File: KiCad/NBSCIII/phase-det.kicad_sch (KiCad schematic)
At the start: 34 parts, among them Q1100 BC337-25, U1 LM324N

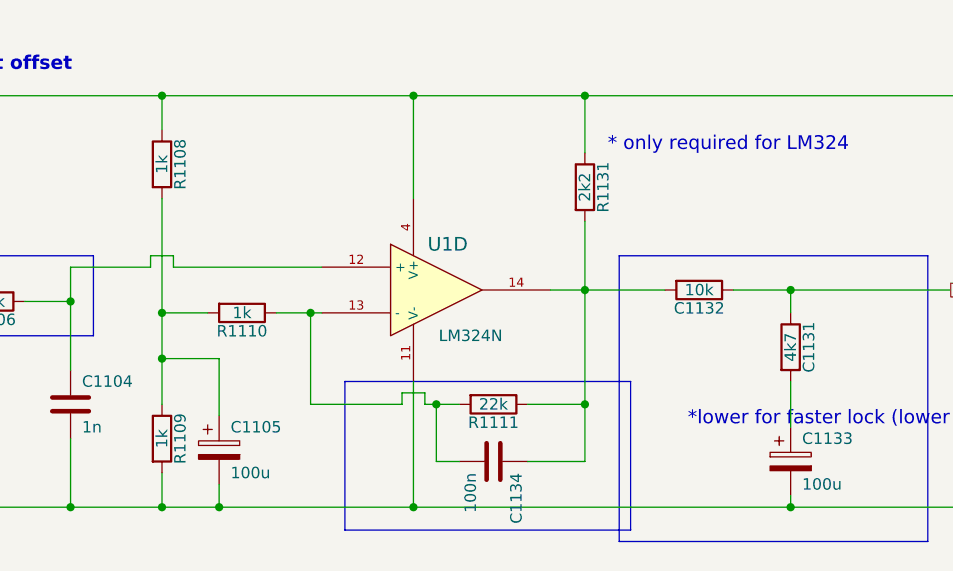
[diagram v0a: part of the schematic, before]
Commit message: derescue lm324
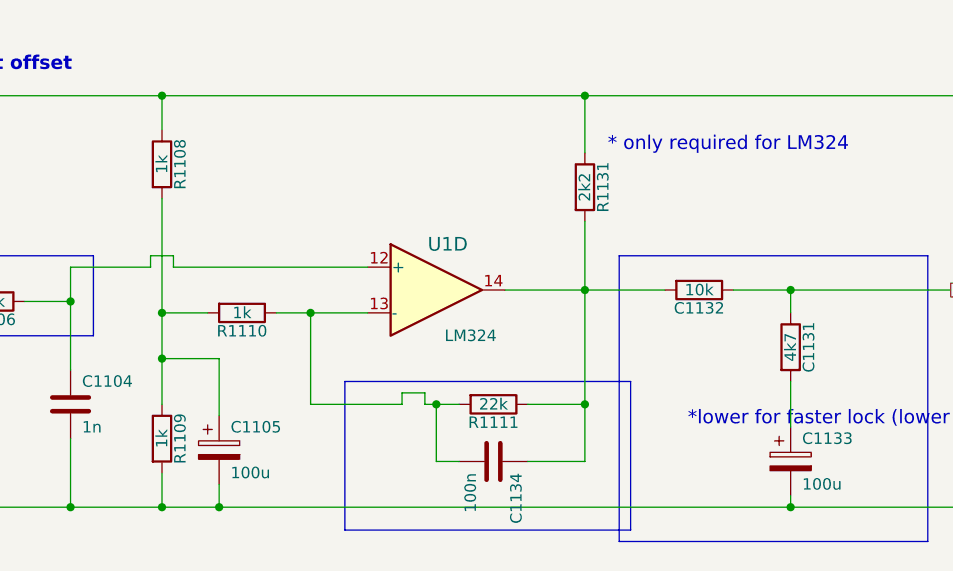
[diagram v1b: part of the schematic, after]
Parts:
- U1: value LM324N -> LM324; symbol NBSCIII-rescue:LM324N -> Amplifier_Operational:LM324
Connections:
- net +12V: no longer U1.4 (V+)
- net GND: no longer U1.11 (V-)
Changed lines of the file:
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@@
   (junction (at 50.8 69.85) (diameter 0) (color 0 0 0 0)
   )
-  (junction (at 179.07 24.13) (diameter 0) (color 0 0 0 0)
-  )
   (junction (at 106.68 46.99) (diameter 0) (color 0 0 0 0)
   )
@@
   (junction (at 220.98 69.85) (diameter 0) (color 0 0 0 0)
   )
-  (junction (at 179.07 69.85) (diameter 0) (color 0 0 0 0)
-  )
   (wire (pts (xy 220.98 69.85) (xy 256.54 69.85))
     (stroke (width 0) (type default) (color 0 0 0 0))
@@
     (stroke (width 0) (type default) (color 0 0 0 0))
   )
+  (wire (pts (xy 152.4 43.18) (xy 173.99 43.18))
+    (stroke (width 0) (type default) (color 0 0 0 0))
+  )
   (wire (pts (xy 151.13 48.26) (xy 156.21 48.26))
     (stroke (width 0) (type default) (color 0 0 0 0))
@@
     (stroke (width 0) (type default) (color 0 0 0 0))
   )
-  (wire (pts (xy 167.64 48.26) (xy 168.91 48.26))
-    (stroke (width 0) (type default) (color 0 0 0 0))
-  )
   (wire (pts (xy 124.46 25.4) (xy 125.73 25.4))
     (stroke (width 0) (type default) (color 0 0 0 0))
@@
     (stroke (width 0) (type default) (color 0 0 0 0))
   )
-  (wire (pts (xy 179.07 55.88) (xy 179.07 69.85))
-    (stroke (width 0) (type default) (color 0 0 0 0))
-  )
   (wire (pts (xy 36.83 46.99) (xy 40.64 46.99))
     (stroke (width 0) (type default) (color 0 0 0 0))
@@
     (stroke (width 0) (type default) (color 0 0 0 0))
   )
-  (wire (pts (xy 157.48 69.85) (xy 179.07 69.85))
+  (wire (pts (xy 157.48 69.85) (xy 220.98 69.85))
     (stroke (width 0) (type default) (color 0 0 0 0))
   )
@@
     (stroke (width 0) (type default) (color 0 0 0 0))
   )
-  (wire (pts (xy 179.07 35.56) (xy 179.07 24.13))
-    (stroke (width 0) (type default) (color 0 0 0 0))
-  )
   (polyline (pts (xy 203.2 55.88) (xy 171.45 55.88))
     (stroke (width 0) (type default) (color 0 0 0 0))
@@
     (stroke (width 0) (type default) (color 0 0 0 0))
   )
-  (wire (pts (xy 198.12 45.72) (xy 194.31 45.72))
+  (wire (pts (xy 189.23 45.72) (xy 198.12 45.72))
     (stroke (width 0) (type default) (color 0 0 0 0))
   )
@@
     (stroke (width 0) (type default) (color 0 0 0 0))
   )
-  (wire (pts (xy 179.07 69.85) (xy 220.98 69.85))
-    (stroke (width 0) (type default) (color 0 0 0 0))
-  )
   (wire (pts (xy 85.09 52.07) (xy 85.09 53.34))
     (stroke (width 0) (type default) (color 0 0 0 0))
   )
-  (wire (pts (xy 152.4 43.18) (xy 168.91 43.18))
-    (stroke (width 0) (type default) (color 0 0 0 0))
-  )
   (wire (pts (xy 77.47 46.99) (xy 72.39 46.99))
     (stroke (width 0) (type default) (color 0 0 0 0))
@@
     (stroke (width 0) (type default) (color 0 0 0 0))
   )
-  (wire (pts (xy 179.07 24.13) (xy 198.12 24.13))
+  (wire (pts (xy 151.13 24.13) (xy 198.12 24.13))
     (stroke (width 0) (type default) (color 0 0 0 0))
   )
@@
     (stroke (width 0) (type default) (color 0 0 0 0))
   )
-  (wire (pts (xy 151.13 24.13) (xy 179.07 24.13))
-    (stroke (width 0) (type default) (color 0 0 0 0))
-  )
   (polyline (pts (xy 201.93 73.66) (xy 236.22 73.66))
     (stroke (width 0) (type default) (color 0 0 0 0))
@@
   )
   (wire (pts (xy 151.13 69.85) (xy 157.48 69.85))
+    (stroke (width 0) (type default) (color 0 0 0 0))
+  )
+  (wire (pts (xy 167.64 48.26) (xy 173.99 48.26))
     (stroke (width 0) (type default) (color 0 0 0 0))
   )
@@
     (pin "2")
   )
-  (symbol (lib_id "NBSCIII-rescue:LM324N") (at 181.61 45.72 0) (unit 4)
+  (symbol (lib_id "Amplifier_Operational:LM324") (at 181.61 45.72 0) (unit 4)
     (in_bom yes) (on_board yes)
     (property "Reference" "U1" (id 0) (at 182.88 40.64 0)
       (effects (font (size 1.524 1.524)))
     )
-    (property "Value" "LM324N" (id 1) (at 185.42 50.8 0))
+    (property "Value" "LM324" (id 1) (at 185.42 50.8 0))
     (property "Footprint" "" (id 2) (at 181.61 45.72 0)
       (effects (font (size 1.27 1.27)) hide)
@@
       (effects (font (size 1.27 1.27)) hide)
     )
-    (pin "11")
-    (pin "4")
     (pin "1")
     (pin "2")
@@
     (pin "13")
     (pin "14")
+    (pin "11")
+    (pin "4")
   )
   (symbol (lib_id "Device:R") (at 151.13 62.23 0) (unit 1)
